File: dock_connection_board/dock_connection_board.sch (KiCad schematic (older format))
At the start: 14 parts, among them J1 USBO, J2 USBI, J3 CHG, J4 I2CI, J5 AUXI, J6 ANI, J7 I2CO, U1 24LC32

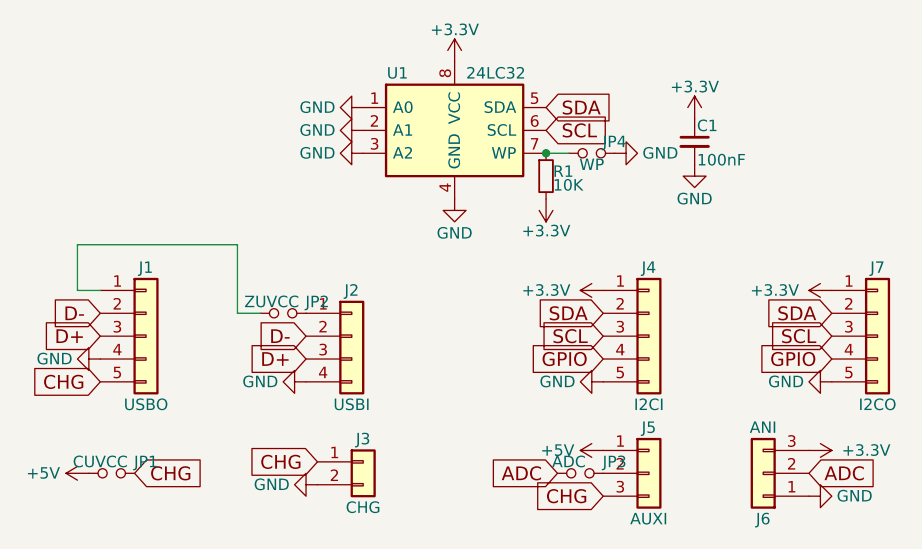
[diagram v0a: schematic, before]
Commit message: Delta dock board finished
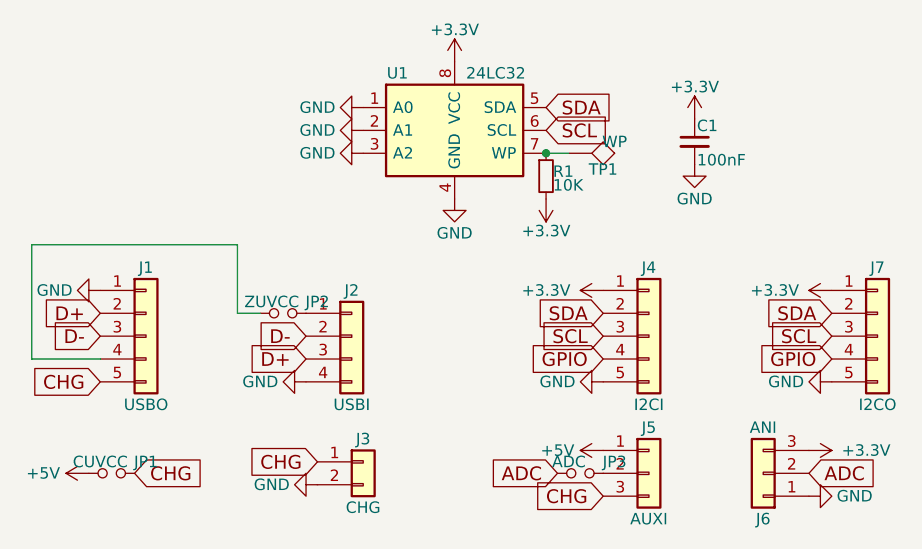
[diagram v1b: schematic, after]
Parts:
- removed JP4: WP, Connect:GS2, symbol Jumper_NO_Small
- added TP1: WP, Measurement_Points:Measurement_Point_Round-SMD-Pad_Small, symbol TEST
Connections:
- net D+: now also J1.2 (Pin_2); no longer J1.3 (Pin_3)
- net D-: now also J1.3 (Pin_3); no longer J1.2 (Pin_2)
- net GND: now also J1.1 (Pin_1); no longer J1.4 (Pin_4)
- net at R1.1, U1.7 (WP): now also TP1.1
- net at JP2.1: now also J1.4 (Pin_4); no longer J1.1 (Pin_1)
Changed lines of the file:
@@
 LIBS:contrib
 LIBS:valves
+LIBS:dock_connection_board-cache
 EELAYER 25 0
 EELAYER END
@@
 SCL
 $Comp
-L Jumper_NO_Small JP4
-U 1 1 5AE7F879
-P 3550 2800
-F 0 "JP4" H 3650 2850 50  0000 C CNN
-F 1 "WP" H 3550 2750 50  0000 C CNN
-F 2 "Connect:GS2" H 3550 2800 50  0001 C CNN
-F 3 "" H 3550 2800 50  0001 C CNN
-	1    3550 2800
-	1    0    0    -1
-$EndComp
-$Comp
 L R_Small R1
 U 1 1 5AE7F8CB
@@
 Connection ~ 3350 2800
 $Comp
-L GND #PWR07
-U 1 1 5AE7F91A
-P 3650 2800
-F 0 "#PWR07" H 3650 2550 50  0001 C CNN
-F 1 "GND" V 3650 2600 50  0000 C CNN
-F 2 "" H 3650 2800 50  0001 C CNN
-F 3 "" H 3650 2800 50  0001 C CNN
-	1    3650 2800
-	0    -1   -1   0
-$EndComp
-$Comp
-L +3.3V #PWR08
+L +3.3V #PWR07
 U 1 1 5AE7F93D
 P 3350 3000
-F 0 "#PWR08" H 3350 2850 50  0001 C CNN
+F 0 "#PWR07" H 3350 2850 50  0001 C CNN
 F 1 "+3.3V" H 3350 3140 50  0000 C CNN
 F 2 "" H 3350 3000 50  0001 C CNN
@@
 $EndComp
 $Comp
-L GND #PWR09
+L GND #PWR08
 U 1 1 5AE7F9C4
 P 2550 2600
-F 0 "#PWR09" H 2550 2350 50  0001 C CNN
+F 0 "#PWR08" H 2550 2350 50  0001 C CNN
 F 1 "GND" V 2550 2400 50  0000 C CNN
 F 2 "" H 2550 2600 50  0001 C CNN
@@
 $EndComp
 $Comp
-L GND #PWR010
+L GND #PWR09
 U 1 1 5AE7F9FD
 P 2550 2700
-F 0 "#PWR010" H 2550 2450 50  0001 C CNN
+F 0 "#PWR09" H 2550 2450 50  0001 C CNN
 F 1 "GND" V 2550 2500 50  0000 C CNN
 F 2 "" H 2550 2700 50  0001 C CNN
@@
 $EndComp
 $Comp
-L GND #PWR011
+L GND #PWR010
 U 1 1 5AE7FA20
 P 2550 2800
-F 0 "#PWR011" H 2550 2550 50  0001 C CNN
+F 0 "#PWR010" H 2550 2550 50  0001 C CNN
 F 1 "GND" V 2550 2600 50  0000 C CNN
 F 2 "" H 2550 2800 50  0001 C CNN
@@
 $EndComp
 $Comp
-L +3.3V #PWR012
+L +3.3V #PWR011
 U 1 1 5AE7FAF5
 P 4000 2650
-F 0 "#PWR012" H 4000 2500 50  0001 C CNN
+F 0 "#PWR011" H 4000 2500 50  0001 C CNN
 F 1 "+3.3V" H 4000 2790 50  0000 C CNN
 F 2 "" H 4000 2650 50  0001 C CNN
@@
 $EndComp
 $Comp
-L GND #PWR013
+L GND #PWR012
 U 1 1 5AE7FB1B
 P 4000 2850
-F 0 "#PWR013" H 4000 2600 50  0001 C CNN
+F 0 "#PWR012" H 4000 2600 50  0001 C CNN
 F 1 "GND" H 4000 2700 50  0000 C CNN
 F 2 "" H 4000 2850 50  0001 C CNN
@@
 $EndComp
 $Comp
-L +3.3V #PWR014
+L +3.3V #PWR013
 U 1 1 5AE7FD1E
 P 4600 3400
-F 0 "#PWR014" H 4600 3250 50  0001 C CNN
+F 0 "#PWR013" H 4600 3250 50  0001 C CNN
 F 1 "+3.3V" V 4600 3650 50  0000 C CNN
 F 2 "" H 4600 3400 50  0001 C CNN
@@
 $EndComp
 $Comp
-L GND #PWR015
+L GND #PWR014
 U 1 1 5AE7FD24
 P 4600 3800
-F 0 "#PWR015" H 4600 3550 50  0001 C CNN
+F 0 "#PWR014" H 4600 3550 50  0001 C CNN
 F 1 "GND" V 4600 3600 50  0000 C CNN
 F 2 "" H 4600 3800 50  0001 C CNN
@@
 GPIO
 $Comp
-L GND #PWR016
+L GND #PWR015
 U 1 1 5AE7FFE1
-P 1400 3700
-F 0 "#PWR016" H 1400 3450 50  0001 C CNN
-F 1 "GND" V 1400 3500 50  0000 C CNN
-F 2 "" H 1400 3700 50  0001 C CNN
-F 3 "" H 1400 3700 50  0001 C CNN
-	1    1400 3700
-	0    1    1    0
-$EndComp
+P 1400 3400
+F 0 "#PWR015" H 1400 3150 50  0001 C CNN
+F 1 "GND" V 1400 3200 50  0000 C CNN
+F 2 "" H 1400 3400 50  0001 C CNN
+F 3 "" H 1400 3400 50  0001 C CNN
+	1    1400 3400
+	0    1    1    0
+$EndComp
+Text GLabel 1400 3500 0    60   Input ~ 0
+D+
 Text GLabel 1400 3600 0    60   Input ~ 0
-D+
-Text GLabel 1400 3500 0    60   Input ~ 0
 D-
 Text GLabel 4500 4200 2    60   Input ~ 0
@@
 ADC
 $Comp
-L +3.3V #PWR017
+L +3.3V #PWR016
 U 1 1 5AE806CA
 P 4500 4100
-F 0 "#PWR017" H 4500 3950 50  0001 C CNN
+F 0 "#PWR016" H 4500 3950 50  0001 C CNN
 F 1 "+3.3V" V 4500 4350 50  0000 C CNN
 F 2 "" H 4500 4100 50  0001 C CNN
@@
 $EndComp
 $Comp
-L +5V #PWR018
+L +5V #PWR017
 U 1 1 5AE80C60
 P 1350 4200
-F 0 "#PWR018" H 1350 4050 50  0001 C CNN
+F 0 "#PWR017" H 1350 4050 50  0001 C CNN
 F 1 "+5V" V 1350 4400 50  0000 C CNN
 F 2 "" H 1350 4200 50  0001 C CNN
@@
 CHG
 $Comp
-L GND #PWR019
+L GND #PWR018
 U 1 1 5AE80E5D
 P 4500 4300
-F 0 "#PWR019" H 4500 4050 50  0001 C CNN
+F 0 "#PWR018" H 4500 4050 50  0001 C CNN
 F 1 "GND" V 4500 4100 50  0000 C CNN
 F 2 "" H 4500 4300 50  0001 C CNN
@@
 $EndComp
 $Comp
-L +5V #PWR020
+L +5V #PWR019
 U 1 1 5AE811B0
 P 3600 4100
-F 0 "#PWR020" H 3600 3950 50  0001 C CNN
+F 0 "#PWR019" H 3600 3950 50  0001 C CNN
 F 1 "+5V" V 3600 4300 50  0000 C CNN
 F 2 "" H 3600 4100 50  0001 C CNN
@@
 CHG
 Wire Wire Line
-	1400 3400 1300 3400
-Wire Wire Line
-	1300 3400 1300 3200
-Wire Wire Line
-	1300 3200 2000 3200
+	1100 3200 2000 3200
 Wire Wire Line
 	2000 3200 2000 3500
+Wire Wire Line
+	1100 3200 1100 3700
+Wire Wire Line
+	1100 3700 1400 3700
+$Comp
+L TEST TP1
+U 1 1 5AEC5E56
+P 3450 2800
+F 0 "TP1" V 3550 2950 50  0000 C BNN
+F 1 "WP" V 3400 3000 50  0000 C CNN
+F 2 "Measurement_Points:Measurement_Point_Round-SMD-Pad_Small" H 3450 2800 50  0001 C CNN
+F 3 "" H 3450 2800 50  0001 C CNN
+	1    3450 2800
+	0    1    1    0
+$EndComp
 $EndSCHEMATC

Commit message: Dock board v1.1 - fixing the dock board outline and positioning
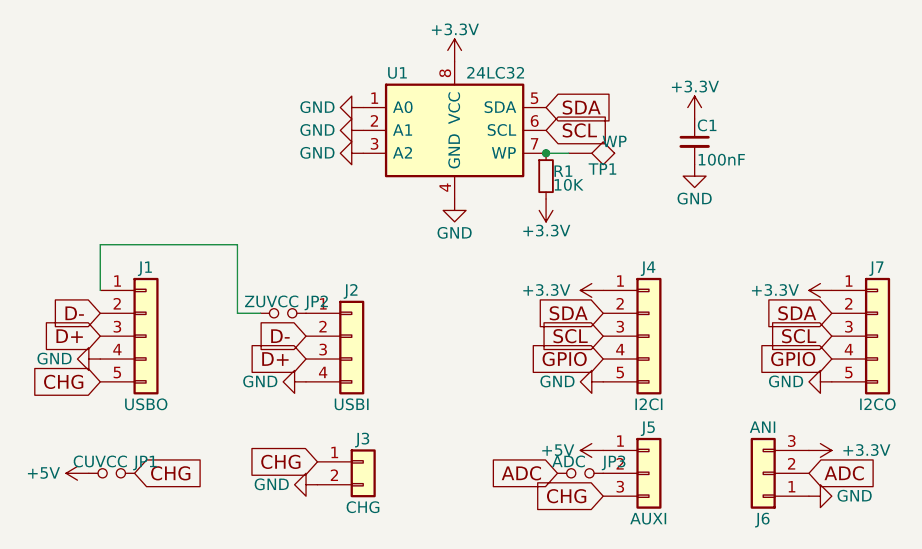
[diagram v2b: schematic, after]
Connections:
- net D+: now also J1.3 (Pin_3); no longer J1.2 (Pin_2)
- net D-: now also J1.2 (Pin_2); no longer J1.3 (Pin_3)
- net GND: now also J1.4 (Pin_4); no longer J1.1 (Pin_1)
- net at JP2.1: now also J1.1 (Pin_1); no longer J1.4 (Pin_4)
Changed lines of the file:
@@
 L GND #PWR015
 U 1 1 5AE7FFE1
-P 1400 3400
-F 0 "#PWR015" H 1400 3150 50  0001 C CNN
-F 1 "GND" V 1400 3200 50  0000 C CNN
-F 2 "" H 1400 3400 50  0001 C CNN
-F 3 "" H 1400 3400 50  0001 C CNN
-	1    1400 3400
+P 1400 3700
+F 0 "#PWR015" H 1400 3450 50  0001 C CNN
+F 1 "GND" V 1400 3500 50  0000 C CNN
+F 2 "" H 1400 3700 50  0001 C CNN
+F 3 "" H 1400 3700 50  0001 C CNN
+	1    1400 3700
 	0    1    1    0
 $EndComp
+Text GLabel 1400 3600 0    60   Input ~ 0
+D+
 Text GLabel 1400 3500 0    60   Input ~ 0
-D+
-Text GLabel 1400 3600 0    60   Input ~ 0
 D-
 Text GLabel 4500 4200 2    60   Input ~ 0
@@
 CHG
 Wire Wire Line
-	1100 3200 2000 3200
-Wire Wire Line
-	2000 3200 2000 3500
-Wire Wire Line
-	1100 3200 1100 3700
-Wire Wire Line
-	1100 3700 1400 3700
+	2000 3500 2000 3200
 $Comp
 L TEST TP1
@@
 	0    1    1    0
 $EndComp
+Wire Wire Line
+	1400 3400 1400 3200
+Wire Wire Line
+	1400 3200 2000 3200
 $EndSCHEMATC
